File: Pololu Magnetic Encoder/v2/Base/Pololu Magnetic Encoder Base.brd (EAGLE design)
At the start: 26.7 x 33.7 mm, 0 parts

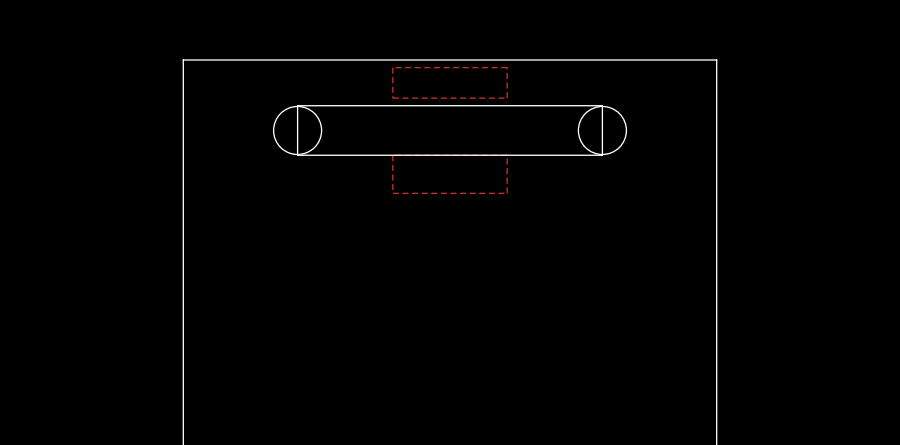
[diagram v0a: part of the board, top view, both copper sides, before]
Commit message: Updated Pololu Magnetic Encoder, fixing pullup issue and adding new silkscreen info
Signed-off-by: Cruz Monrreal II <Cruz.Monrreal@gmail.com>
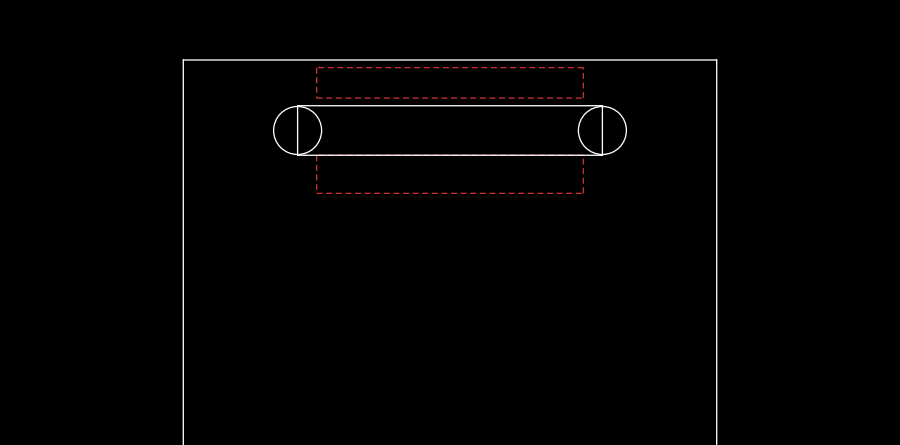
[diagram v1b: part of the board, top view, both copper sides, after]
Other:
- board text added: "Cruz Monrreal II"
- board text added: "innovativemaker.com"
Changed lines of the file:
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@@
 <?xml version="1.0" encoding="utf-8"?>
 <!DOCTYPE eagle SYSTEM "eagle.dtd">
-<eagle version="6.1">
+<eagle version="6.3">
 <drawing>
 <settings>
@@
 <wire x1="6.096" y1="8.89" x2="5.08" y2="8.89" width="0" layer="20"/>
 <wire x1="21.844" y1="8.89" x2="22.86" y2="8.89" width="0" layer="20"/>
-<rectangle x1="12.065" y1="29.21" x2="15.875" y2="30.48" layer="29"/>
-<rectangle x1="12.065" y1="32.131" x2="15.875" y2="33.401" layer="29"/>
+<rectangle x1="9.525" y1="32.131" x2="18.415" y2="33.401" layer="29"/>
+<rectangle x1="9.525" y1="29.21" x2="18.415" y2="30.48" layer="29" rot="R180"/>
+<text x="13.97" y="1.905" size="0.8128" layer="52" font="vector" ratio="12" rot="MR0" align="bottom-center">Cruz Monrreal II</text>
+<text x="13.97" y="0.635" size="0.8128" layer="52" font="vector" ratio="12" rot="MR0" align="bottom-center">innovativemaker.com</text>
 </plain>
 <attributes>
@@
 </class>
 </classes>
-<designrules>
+<designrules name="default">
 <description language="de">&lt;b&gt;EAGLE Design Rules&lt;/b&gt;
 &lt;p&gt;
@@
 <signal name="GND">
 <polygon width="0.4064" layer="1">
-<vertex x="12.065" y="29.21"/>
-<vertex x="15.875" y="29.21"/>
-<vertex x="15.875" y="30.48"/>
-<vertex x="12.065" y="30.48"/>
+<vertex x="9.525" y="29.21"/>
+<vertex x="18.415" y="29.21"/>
+<vertex x="18.415" y="30.48"/>
+<vertex x="9.525" y="30.48"/>
 </polygon>
 <polygon width="0.4064" layer="1">
-<vertex x="12.065" y="32.385"/>
-<vertex x="15.875" y="32.385"/>
-<vertex x="15.875" y="33.401"/>
-<vertex x="12.065" y="33.401"/>
+<vertex x="9.525" y="32.385"/>
+<vertex x="18.415" y="32.385"/>
+<vertex x="18.415" y="33.401"/>
+<vertex x="9.525" y="33.401"/>
 </polygon>
 </signal>
